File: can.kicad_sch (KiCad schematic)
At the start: 8 parts, among them J6 Conn_02x03_Odd_Even, U7 SN65HVD230

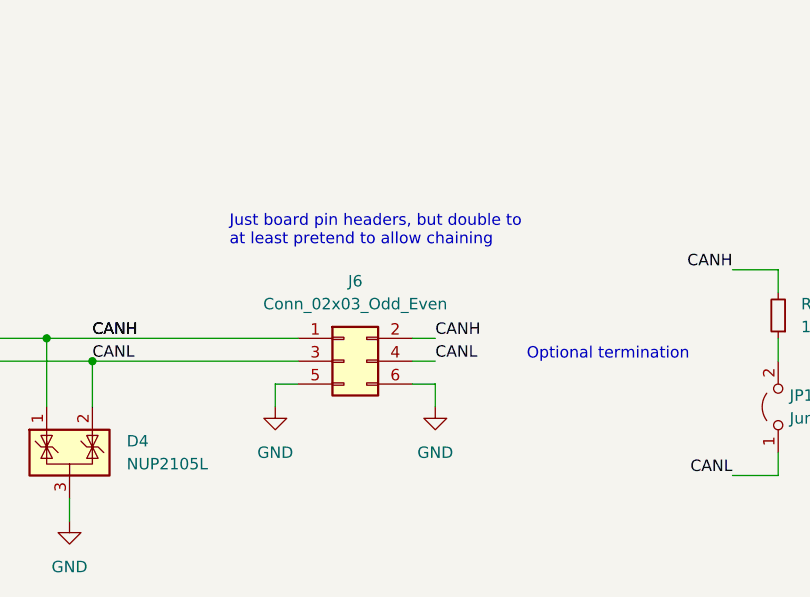
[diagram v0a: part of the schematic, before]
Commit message: unrouted: 0
Juggled all the key matrix IOs and reviewed "all" outstanding TODOs

left: add another cap for downstream Vbus.  it's free, and can only
help.

left: lots of silk?
left: place as much free io to pads as can be easily done, for
test/board reuse.
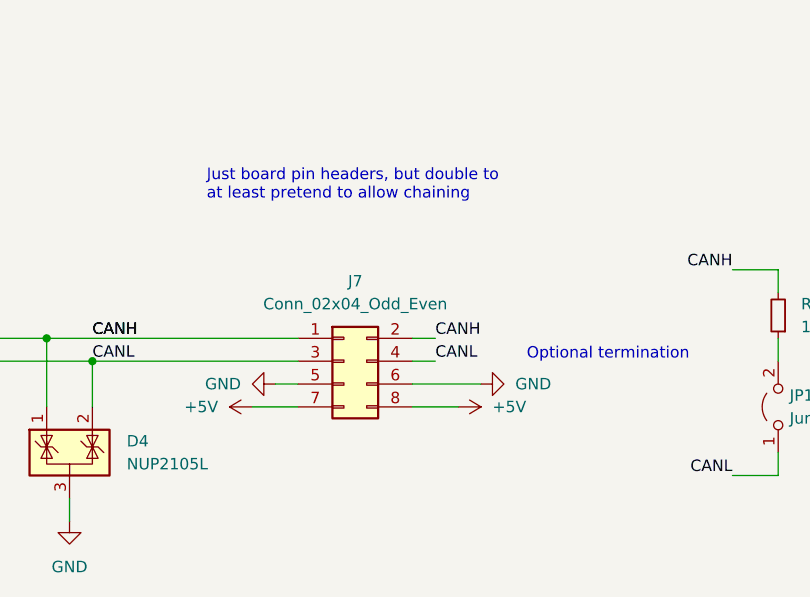
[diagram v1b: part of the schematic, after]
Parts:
- removed J6: Conn_02x03_Odd_Even, Connector_PinHeader_2.54mm:PinHeader_2x03_P2.54mm_Vertical, symbol Connector_Generic:Conn_02x03_Odd_Even
- added J7: Conn_02x04_Odd_Even, Connector_PinHeader_2.54mm:PinHeader_2x04_P2.54mm_Vertical, symbol Connector_Generic:Conn_02x04_Odd_Even
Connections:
- net CANH: now also J7.1 (Pin_1), J7.2 (Pin_2)
- net CANL: now also J7.3 (Pin_3), J7.4 (Pin_4)
- net GND: now also J7.5 (Pin_5), J7.6 (Pin_6)
- new net +5V: J7.7 (Pin_7), J7.8 (Pin_8)
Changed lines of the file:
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@@
-    (stroke (width 0) (type default))
-  )
-  (wire (pts (xy 177.8 104.14) (xy 175.26 104.14))
     (stroke (width 0) (type default))
   )
@@
     (stroke (width 0) (type default))
   )
+  (wire (pts (xy 190.5 106.68) (xy 195.58 106.68))
+    (stroke (width 0) (type default))
+  )
   (wire (pts (xy 149.86 99.06) (xy 149.86 106.68))
     (stroke (width 0) (type default))
@@
     (stroke (width 0) (type default))
   )
-  (wire (pts (xy 175.26 104.14) (xy 175.26 106.68))
-    (stroke (width 0) (type default))
-  )
   (wire (pts (xy 139.7 99.06) (xy 149.86 99.06))
     (stroke (width 0) (type default))
@@
     (stroke (width 0) (type default))
   )
+  (wire (pts (xy 172.72 106.68) (xy 177.8 106.68))
+    (stroke (width 0) (type default))
+  )
   (wire (pts (xy 139.7 101.6) (xy 154.94 101.6))
     (stroke (width 0) (type default))
   )
-  (wire (pts (xy 190.5 104.14) (xy 193.04 104.14))
-    (stroke (width 0) (type default))
-  )
   (wire (pts (xy 106.68 104.14) (xy 111.76 104.14))
     (stroke (width 0) (type default))
@@
     (stroke (width 0) (type default))
   )
+  (wire (pts (xy 175.26 104.14) (xy 177.8 104.14))
+    (stroke (width 0) (type default))
+  )
+  (wire (pts (xy 190.5 104.14) (xy 198.12 104.14))
+    (stroke (width 0) (type default))
+  )
   (wire (pts (xy 106.68 99.06) (xy 119.38 99.06))
     (stroke (width 0) (type default))
   )
-  (wire (pts (xy 193.04 104.14) (xy 193.04 106.68))
-    (stroke (width 0) (type default))
-  )
   (wire (pts (xy 154.94 101.6) (xy 177.8 101.6))
     (stroke (width 0) (type default))
@@
   )
   (text "Just board pin headers, but double to\nat least pretend to allow chaining"
-    (at 170.18 88.9 0)
+    (at 167.64 83.82 0)
     (effects (font (size 1.27 1.27)) (justify left bottom))
   )
@@
     (effects (font (size 1.27 1.27)) (justify right))
   )
+  (symbol (lib_id "Connector_Generic:Conn_02x04_Odd_Even") (at 182.88 101.6 0) (unit 1)
+    (in_bom yes) (on_board yes) (dnp no) (fields_autoplaced)
+    (property "Reference" "J7" (at 184.15 92.71 0)
+      (effects (font (size 1.27 1.27)))
+    )
+    (property "Value" "Conn_02x04_Odd_Even" (at 184.15 95.25 0)
+      (effects (font (size 1.27 1.27)))
+    )
+    (property "Footprint" "Connector_PinHeader_2.54mm:PinHeader_2x04_P2.54mm_Vertical" (at 182.88 101.6 0)
+      (effects (font (size 1.27 1.27)) hide)
+    )
+    (property "Datasheet" "~" (at 182.88 101.6 0)
+      (effects (font (size 1.27 1.27)) hide)
+    )
+    (pin "5")
+    (pin "3")
+    (pin "2")
+    (pin "6")
+    (pin "4")
+    (pin "7")
+    (pin "1")
+    (pin "8")
+    (instances
+      (project "das-kb4-bara2"
+        (path "/d0e4eaec-96cb-4a0e-a384-5b3e3f5f8d5d/a2d5569b-3e38-48fc-9c53-ff19306ffa54"
+          (reference "J7") (unit 1)
+        )
+      )
+    )
+  )
   (symbol (lib_id "Power_Protection:NUP2105L") (at 152.4 111.76 0) (unit 1)
     (in_bom yes) (on_board yes) (dnp no) (fields_autoplaced)
@@
         (path "/d0e4eaec-96cb-4a0e-a384-5b3e3f5f8d5d/a2d5569b-3e38-48fc-9c53-ff19306ffa54"
           (reference "R19") (unit 1)
+        )
+      )
+    )
+  )
+  (symbol (lib_id "power:+5V") (at 172.72 106.68 90) (unit 1)
+    (in_bom yes) (on_board yes) (dnp no) (fields_autoplaced)
+    (property "Reference" "#PWR053" (at 176.53 106.68 0)
+      (effects (font (size 1.27 1.27)) hide)
+    )
+    (property "Value" "+5V" (at 168.91 106.68 90)
+      (effects (font (size 1.27 1.27)) (justify left))
+    )
+    (property "Footprint" "" (at 172.72 106.68 0)
+      (effects (font (size 1.27 1.27)) hide)
+    )
+    (property "Datasheet" "" (at 172.72 106.68 0)
+      (effects (font (size 1.27 1.27)) hide)
+    )
+    (pin "1")
+    (instances
+      (project "das-kb4-bara2"
+        (path "/d0e4eaec-96cb-4a0e-a384-5b3e3f5f8d5d/a2d5569b-3e38-48fc-9c53-ff19306ffa54"
+          (reference "#PWR053") (unit 1)
         )
       )
@@
     )
   )
-  (symbol (lib_id "power:GND") (at 175.26 106.68 0) (unit 1)
-    (in_bom yes) (on_board yes) (dnp no) (fields_autoplaced)
-    (property "Reference" "#PWR046" (at 175.26 113.03 0)
-      (effects (font (size 1.27 1.27)) hide)
-    )
-    (property "Value" "GND" (at 175.26 111.76 0)
-      (effects (font (size 1.27 1.27)))
-    )
-    (property "Footprint" "" (at 175.26 106.68 0)
-      (effects (font (size 1.27 1.27)) hide)
-    )
-    (property "Datasheet" "" (at 175.26 106.68 0)
+  (symbol (lib_id "power:GND") (at 175.26 104.14 270) (unit 1)
+    (in_bom yes) (on_board yes) (dnp no) (fields_autoplaced)
+    (property "Reference" "#PWR046" (at 168.91 104.14 0)
+      (effects (font (size 1.27 1.27)) hide)
+    )
+    (property "Value" "GND" (at 171.45 104.14 90)
+      (effects (font (size 1.27 1.27)) (justify right))
+    )
+    (property "Footprint" "" (at 175.26 104.14 0)
+      (effects (font (size 1.27 1.27)) hide)
+    )
+    (property "Datasheet" "" (at 175.26 104.14 0)
       (effects (font (size 1.27 1.27)) hide)
     )
@@
         (path "/d0e4eaec-96cb-4a0e-a384-5b3e3f5f8d5d/a2d5569b-3e38-48fc-9c53-ff19306ffa54"
           (reference "#PWR048") (unit 1)
-        )
-      )
-    )
-  )
-  (symbol (lib_id "Connector_Generic:Conn_02x03_Odd_Even") (at 182.88 101.6 0) (unit 1)
-    (in_bom yes) (on_board yes) (dnp no) (fields_autoplaced)
-    (property "Reference" "J6" (at 184.15 92.71 0)
-      (effects (font (size 1.27 1.27)))
-    )
-    (property "Value" "Conn_02x03_Odd_Even" (at 184.15 95.25 0)
-      (effects (font (size 1.27 1.27)))
-    )
-    (property "Footprint" "Connector_PinHeader_2.54mm:PinHeader_2x03_P2.54mm_Vertical" (at 182.88 101.6 0)
-      (effects (font (size 1.27 1.27)) hide)
-    )
-    (property "Datasheet" "~" (at 182.88 101.6 0)
-      (effects (font (size 1.27 1.27)) hide)
-    )
-    (pin "1")
-    (pin "4")
-    (pin "5")
-    (pin "6")
-    (pin "3")
-    (pin "2")
-    (instances
-      (project "das-kb4-bara2"
-        (path "/d0e4eaec-96cb-4a0e-a384-5b3e3f5f8d5d/7c81bc9d-f306-4c7f-90ce-10f7b22818e4"
-          (reference "J6") (unit 1)
-        )
-        (path "/d0e4eaec-96cb-4a0e-a384-5b3e3f5f8d5d/a2d5569b-3e38-48fc-9c53-ff19306ffa54"
-          (reference "J6") (unit 1)
         )
       )
@@
     )
   )
-  (symbol (lib_id "power:GND") (at 193.04 106.68 0) (unit 1)
-    (in_bom yes) (on_board yes) (dnp no) (fields_autoplaced)
-    (property "Reference" "#PWR046" (at 193.04 113.03 0)
-      (effects (font (size 1.27 1.27)) hide)
-    )
-    (property "Value" "GND" (at 193.04 111.76 0)
-      (effects (font (size 1.27 1.27)))
-    )
-    (property "Footprint" "" (at 193.04 106.68 0)
-      (effects (font (size 1.27 1.27)) hide)
-    )
-    (property "Datasheet" "" (at 193.04 106.68 0)
+  (symbol (lib_id "power:GND") (at 198.12 104.14 90) (unit 1)
+    (in_bom yes) (on_board yes) (dnp no) (fields_autoplaced)
+    (property "Reference" "#PWR046" (at 204.47 104.14 0)
+      (effects (font (size 1.27 1.27)) hide)
+    )
+    (property "Value" "GND" (at 201.93 104.14 90)
+      (effects (font (size 1.27 1.27)) (justify right))
+    )
+    (property "Footprint" "" (at 198.12 104.14 0)
+      (effects (font (size 1.27 1.27)) hide)
+    )
+    (property "Datasheet" "" (at 198.12 104.14 0)
       (effects (font (size 1.27 1.27)) hide)
     )
@@
         )
       )
+    )
+  )
+  (symbol (lib_id "power:+5V") (at 195.58 106.68 270) (unit 1)
+    (in_bom yes) (on_board yes) (dnp no) (fields_autoplaced)
+    (property "Reference" "#PWR054" (at 191.77 106.68 0)
+      (effects (font (size 1.27 1.27)) hide)
+    )
+    (property "Value" "+5V" (at 199.39 106.68 90)
+      (effects (font (size 1.27 1.27)) (justify left))
+    )
+    (property "Footprint" "" (at 195.58 106.68 0)
+      (effects (font (size 1.27 1.27)) hide)
+    )
+    (property "Datasheet" "" (at 195.58 106.68 0)
+      (effects (font (size 1.27 1.27)) hide)
+    )
+    (pin "1")
+    (instances
+      (project "das-kb4-bara2"
+        (path "/d0e4eaec-96cb-4a0e-a384-5b3e3f5f8d5d/a2d5569b-3e38-48fc-9c53-ff19306ffa54"
+          (reference "#PWR054") (unit 1)
+        )
+      )

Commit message: fix some erc/drc
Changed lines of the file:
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@@
   (junction (at 154.94 101.6) (diameter 0) (color 0 0 0 0)
   )
+  (junction (at 129.54 86.36) (diameter 0) (color 0 0 0 0)
+  )
   (no_connect (at 119.38 101.6))
+  (wire (pts (xy 121.92 83.82) (xy 121.92 86.36))
+    (stroke (width 0) (type default))
+  )
   (wire (pts (xy 152.4 119.38) (xy 152.4 116.84))
+    (stroke (width 0) (type default))
+  )
+  (wire (pts (xy 121.92 86.36) (xy 129.54 86.36))
     (stroke (width 0) (type default))
   )
@@
         )
       )
+    )
+  )
+  (symbol (lib_id "power:PWR_FLAG") (at 121.92 83.82 0) (unit 1)
+    (in_bom yes) (on_board yes) (dnp no) (fields_autoplaced)
+    (property "Reference" "#FLG01" (at 121.92 81.915 0)
+      (effects (font (size 1.27 1.27)) hide)
+    )
+    (property "Value" "PWR_FLAG" (at 121.92 78.74 0)
+      (effects (font (size 1.27 1.27)))
+    )
+    (property "Footprint" "" (at 121.92 83.82 0)
+      (effects (font (size 1.27 1.27)) hide)
+    )
+    (property "Datasheet" "~" (at 121.92 83.82 0)
+      (effects (font (size 1.27 1.27)) hide)
+    )
+    (pin "1")
+    (instances
+      (project "das-kb4-bara2"
+        (path "/d0e4eaec-96cb-4a0e-a384-5b3e3f5f8d5d/f457a5c4-270e-459d-a4f0-150cf90e3909"
+          (reference "#FLG01") (unit 1)
+        )
+        (path "/d0e4eaec-96cb-4a0e-a384-5b3e3f5f8d5d/a2d5569b-3e38-48fc-9c53-ff19306ffa54"
+          (reference "#FLG04") (unit 1)
+        )
+      )
